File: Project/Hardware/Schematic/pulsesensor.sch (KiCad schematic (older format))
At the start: 2 parts

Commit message: Fixa bibliotek ref
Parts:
- U?: symbol lab-rescue:Pulse_sensor-PASC -> PASC:Pulse_sensor
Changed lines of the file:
@@
 $EndDescr
 $Comp
-L lab-rescue:Pulse_sensor-PASC U?
+L PASC:Pulse_sensor U?
 U 1 1 5C5DA663
 P 5700 3400

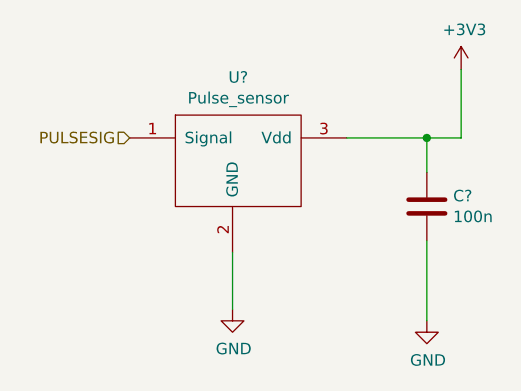
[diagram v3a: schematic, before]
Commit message: Tog bort power supply +7, lade till switch för att switcha mellan batteri och USB power. Lade till power-net symbol för oregulerad supply voltage +VIN.
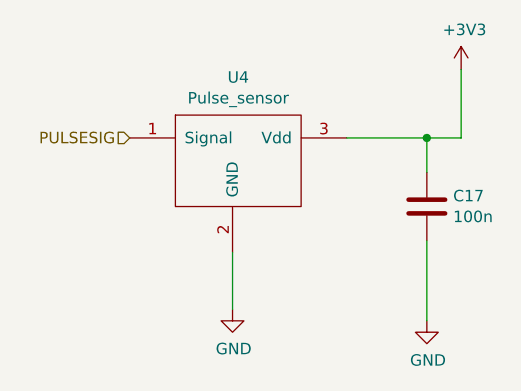
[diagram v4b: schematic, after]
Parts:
- gave numbers to parts that had none: 2
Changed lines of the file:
@@
 $EndDescr
 $Comp
-L PASC:Pulse_sensor U?
+L PASC:Pulse_sensor U4
 U 1 1 5C5DA663
 P 5700 3400
-F 0 "U?" H 5725 3765 50  0000 C CNN
+F 0 "U4" H 5725 3765 50  0000 C CNN
 F 1 "Pulse_sensor" H 5725 3674 50  0000 C CNN
 F 2 "Pin_Headers:Pin_Header_Straight_1x03_Pitch2.54mm" H 5700 3400 50  0001 C CNN
@@
 $EndComp
 $Comp
-L power:+3V3 #PWR?
+L power:+3V3 #PWR0125
 U 1 1 5C5DA797
 P 6700 3000
-F 0 "#PWR?" H 6700 2850 50  0001 C CNN
+F 0 "#PWR0125" H 6700 2850 50  0001 C CNN
 F 1 "+3V3" H 6715 3173 50  0000 C CNN
 F 2 "" H 6700 3000 50  0001 C CNN
@@
 $EndComp
 $Comp
-L Device:C C?
+L Device:C C17
 U 1 1 5C5DA7DA
 P 6550 3600
-F 0 "C?" H 6665 3646 50  0000 L CNN
+F 0 "C17" H 6665 3646 50  0000 L CNN
 F 1 "100n" H 6665 3555 50  0000 L CNN
 F 2 "" H 6588 3450 50  0001 C CNN
@@
 	6700 3300 6700 3000
 $Comp
-L power:GND #PWR?
+L power:GND #PWR0126
 U 1 1 5C5DA906
 P 5700 4050
-F 0 "#PWR?" H 5700 3800 50  0001 C CNN
+F 0 "#PWR0126" H 5700 3800 50  0001 C CNN
 F 1 "GND" H 5705 3877 50  0000 C CNN
 F 2 "" H 5700 4050 50  0001 C CNN
@@
 $EndComp
 $Comp
-L power:GND #PWR?
+L power:GND #PWR0127
 U 1 1 5C5DA96D
 P 6550 4100
-F 0 "#PWR?" H 6550 3850 50  0001 C CNN
+F 0 "#PWR0127" H 6550 3850 50  0001 C CNN
 F 1 "GND" H 6555 3927 50  0000 C CNN
 F 2 "" H 6550 4100 50  0001 C CNN

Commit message: Intermediate...
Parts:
- C17: footprint (none) -> Capacitor_SMD:C_0805_2012Metric_Pad1.15x1.40mm_HandSolder
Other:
- moved on the sheet: C17, U4
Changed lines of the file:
@@
 EELAYER 26 0
 EELAYER END
-$Descr A4 11693 8268
+$Descr User 5512 5512
 encoding utf-8
 Sheet 3 7
 Title ""
-Date ""
-Rev ""
-Comp ""
+Date "2019-02-12"
+Rev "1"
+Comp "PASC"
 Comment1 ""
 Comment2 ""
@@
 L PASC:Pulse_sensor U4
 U 1 1 5C5DA663
-P 5700 3400
-F 0 "U4" H 5725 3765 50  0000 C CNN
-F 1 "Pulse_sensor" H 5725 3674 50  0000 C CNN
-F 2 "Pin_Headers:Pin_Header_Straight_1x03_Pitch2.54mm" H 5700 3400 50  0001 C CNN
-F 3 "" H 5700 3400 50  0001 C CNN
-	1    5700 3400
+P 2400 1900
+F 0 "U4" H 2425 2265 50  0000 C CNN
+F 1 "Pulse_sensor" H 2425 2174 50  0000 C CNN
+F 2 "Pin_Headers:Pin_Header_Straight_1x03_Pitch2.54mm" H 2400 1900 50  0001 C CNN
+F 3 "" H 2400 1900 50  0001 C CNN
+	1    2400 1900
 	1    0    0    -1
 $EndComp
@@
 L power:+3V3 #PWR0125
 U 1 1 5C5DA797
-P 6700 3000
-F 0 "#PWR0125" H 6700 2850 50  0001 C CNN
-F 1 "+3V3" H 6715 3173 50  0000 C CNN
-F 2 "" H 6700 3000 50  0001 C CNN
-F 3 "" H 6700 3000 50  0001 C CNN
-	1    6700 3000
+P 3400 1500
+F 0 "#PWR0125" H 3400 1350 50  0001 C CNN
+F 1 "+3V3" H 3415 1673 50  0000 C CNN
+F 2 "" H 3400 1500 50  0001 C CNN
+F 3 "" H 3400 1500 50  0001 C CNN
+	1    3400 1500
 	1    0    0    -1
 $EndComp
@@
 L Device:C C17
 U 1 1 5C5DA7DA
-P 6550 3600
-F 0 "C17" H 6665 3646 50  0000 L CNN
-F 1 "100n" H 6665 3555 50  0000 L CNN
-F 2 "" H 6588 3450 50  0001 C CNN
-F 3 "~" H 6550 3600 50  0001 C CNN
-	1    6550 3600
+P 3250 2100
+F 0 "C17" H 3365 2146 50  0000 L CNN
+F 1 "100n" H 3365 2055 50  0000 L CNN
+F 2 "Capacitor_SMD:C_0805_2012Metric_Pad1.15x1.40mm_HandSolder" H 3288 1950 50  0001 C CNN
+F 3 "~" H 3250 2100 50  0001 C CNN
+	1    3250 2100
 	1    0    0    -1
 $EndComp
 Wire Wire Line
-	6200 3300 6550 3300
+	2900 1800 3250 1800
 Wire Wire Line
-	6700 3300 6700 3000
+	3400 1800 3400 1500
 $Comp
 L power:GND #PWR0126
 U 1 1 5C5DA906
-P 5700 4050
-F 0 "#PWR0126" H 5700 3800 50  0001 C CNN
-F 1 "GND" H 5705 3877 50  0000 C CNN
-F 2 "" H 5700 4050 50  0001 C CNN
-F 3 "" H 5700 4050 50  0001 C CNN
-	1    5700 4050
+P 2400 2550
+F 0 "#PWR0126" H 2400 2300 50  0001 C CNN
+F 1 "GND" H 2405 2377 50  0000 C CNN
+F 2 "" H 2400 2550 50  0001 C CNN
+F 3 "" H 2400 2550 50  0001 C CNN
+	1    2400 2550
 	1    0    0    -1
 $EndComp
@@
 L power:GND #PWR0127
 U 1 1 5C5DA96D
-P 6550 4100
-F 0 "#PWR0127" H 6550 3850 50  0001 C CNN
-F 1 "GND" H 6555 3927 50  0000 C CNN
-F 2 "" H 6550 4100 50  0001 C CNN
-F 3 "" H 6550 4100 50  0001 C CNN
-	1    6550 4100
+P 3250 2600
+F 0 "#PWR0127" H 3250 2350 50  0001 C CNN
+F 1 "GND" H 3255 2427 50  0000 C CNN
+F 2 "" H 3250 2600 50  0001 C CNN
+F 3 "" H 3250 2600 50  0001 C CNN
+	1    3250 2600
 	1    0    0    -1
 $EndComp
 Wire Wire Line
-	6550 3750 6550 4100
+	3250 2250 3250 2600
 Wire Wire Line
-	6550 3450 6550 3300
-Connection ~ 6550 3300
+	3250 1950 3250 1800
+Connection ~ 3250 1800
 Wire Wire Line
-	6550 3300 6700 3300
+	3250 1800 3400 1800
 Wire Wire Line
-	5700 3800 5700 4050
-Text HLabel 5250 3300 0    50   Input ~ 0
+	2400 2300 2400 2550
+Text HLabel 1950 1800 0    50   Input ~ 0
 PULSESIG
 $EndSCHEMATC
